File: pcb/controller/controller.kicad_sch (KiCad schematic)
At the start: 16 parts, among them J1 Barrel_Jack, J2 AVR-ISP-6, U1 ATmega328P-A, Y1 Crystal_GND24

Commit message: More Controller Updates
Continuing to work on the controller board schematic
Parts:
- added JBUZZ1: Conn_01x02_Male, Connector_JST:JST_PH_B2B-PH-K_1x02_P2.00mm_Vertical, symbol Connector:Conn_01x02_Male
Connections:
- net GND: now also JBUZZ1.1 (Pin_1)
- net at U1.14 (PB2): now also JBUZZ1.2 (Pin_2)
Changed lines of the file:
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@@
+    (stroke (width 0) (type default) (color 0 0 0 0))
+  )
+  (wire (pts (xy 168.91 43.18) (xy 168.91 63.5))
     (stroke (width 0) (type default) (color 0 0 0 0))
   )
@@
     (stroke (width 0) (type default) (color 0 0 0 0))
   )
+  (wire (pts (xy 205.74 34.29) (xy 205.74 36.83))
+    (stroke (width 0) (type default) (color 0 0 0 0))
+  )
   (wire (pts (xy 180.34 71.12) (xy 180.34 99.06))
     (stroke (width 0) (type default) (color 0 0 0 0))
   )
+  (wire (pts (xy 168.91 63.5) (xy 154.94 63.5))
+    (stroke (width 0) (type default) (color 0 0 0 0))
+  )
   (wire (pts (xy 166.37 31.75) (xy 166.37 60.96))
     (stroke (width 0) (type default) (color 0 0 0 0))
@@
     (stroke (width 0) (type default) (color 0 0 0 0))
   )
+  (wire (pts (xy 168.91 43.18) (xy 203.2 43.18))
+    (stroke (width 0) (type default) (color 0 0 0 0))
+  )
   (wire (pts (xy 154.94 71.12) (xy 180.34 71.12))
     (stroke (width 0) (type default) (color 0 0 0 0))
@@
   )
   (wire (pts (xy 180.34 99.06) (xy 182.88 99.06))
+    (stroke (width 0) (type default) (color 0 0 0 0))
+  )
+  (wire (pts (xy 203.2 34.29) (xy 203.2 43.18))
     (stroke (width 0) (type default) (color 0 0 0 0))
   )
@@
     (pin "1")
   )
+  (symbol (lib_id "Connector:Conn_01x02_Male") (at 205.74 29.21 270) (unit 1)
+    (in_bom yes) (on_board yes) (fields_autoplaced)
+    (property "Reference" "JBUZZ1" (id 0) (at 207.01 28.5749 90)
+      (effects (font (size 1.27 1.27)) (justify left))
+    )
+    (property "Value" "Conn_01x02_Male" (id 1) (at 207.01 31.1149 90)
+      (effects (font (size 1.27 1.27)) (justify left))
+    )
+    (property "Footprint" "Connector_JST:JST_PH_B2B-PH-K_1x02_P2.00mm_Vertical" (id 2) (at 205.74 29.21 0)
+      (effects (font (size 1.27 1.27)) hide)
+    )
+    (property "Datasheet" "~" (id 3) (at 205.74 29.21 0)
+      (effects (font (size 1.27 1.27)) hide)
+    )
+    (pin "1")
+    (pin "2")
+  )
   (symbol (lib_id "power:GND") (at 172.72 34.29 0) (unit 1)
     (in_bom yes) (on_board yes) (fields_autoplaced)
@@
     (pin "3")
   )
+  (symbol (lib_id "power:GND") (at 205.74 36.83 0) (unit 1)
+    (in_bom yes) (on_board yes) (fields_autoplaced)
+    (property "Reference" "#PWR0118" (id 0) (at 205.74 43.18 0)
+      (effects (font (size 1.27 1.27)) hide)
+    )
+    (property "Value" "GND" (id 1) (at 205.74 41.91 0))
+    (property "Footprint" "" (id 2) (at 205.74 36.83 0)
+      (effects (font (size 1.27 1.27)) hide)
+    )
+    (property "Datasheet" "" (id 3) (at 205.74 36.83 0)
+      (effects (font (size 1.27 1.27)) hide)
+    )
+    (pin "1")
+  )
   (symbol (lib_id "Connector:Conn_01x03_Male") (at 234.95 58.42 180) (unit 1)
     (in_bom yes) (on_board yes)
@@
       (reference "#PWR0117") (unit 1) (value "GND") (footprint "")
     )
+    (path "/b5b62e28-9fc8-463e-a7f1-aa7597965c9b"
+      (reference "#PWR0118") (unit 1) (value "GND") (footprint "")
+    )
     (path "/7f74c263-cca2-4e4e-8840-c701f7c98d5f"
       (reference "#PWR0119") (unit 1) (value "+5V") (footprint "")
@@
       (reference "J2") (unit 1) (value "AVR-ISP-6") (footprint "Connector_IDC:IDC-Header_2x03_P2.54mm_Vertical")
     )
+    (path "/6588fbb0-09c1-440c-88e5-9c03bc8e1ab7"
+      (reference "JBUZZ1") (unit 1) (value "Conn_01x02_Male") (footprint "Connector_JST:JST_PH_B2B-PH-K_1x02_P2.00mm_Vertical")
+    )
     (path "/8f4ef035-8269-4652-85c4-8eb26bfa3f71"

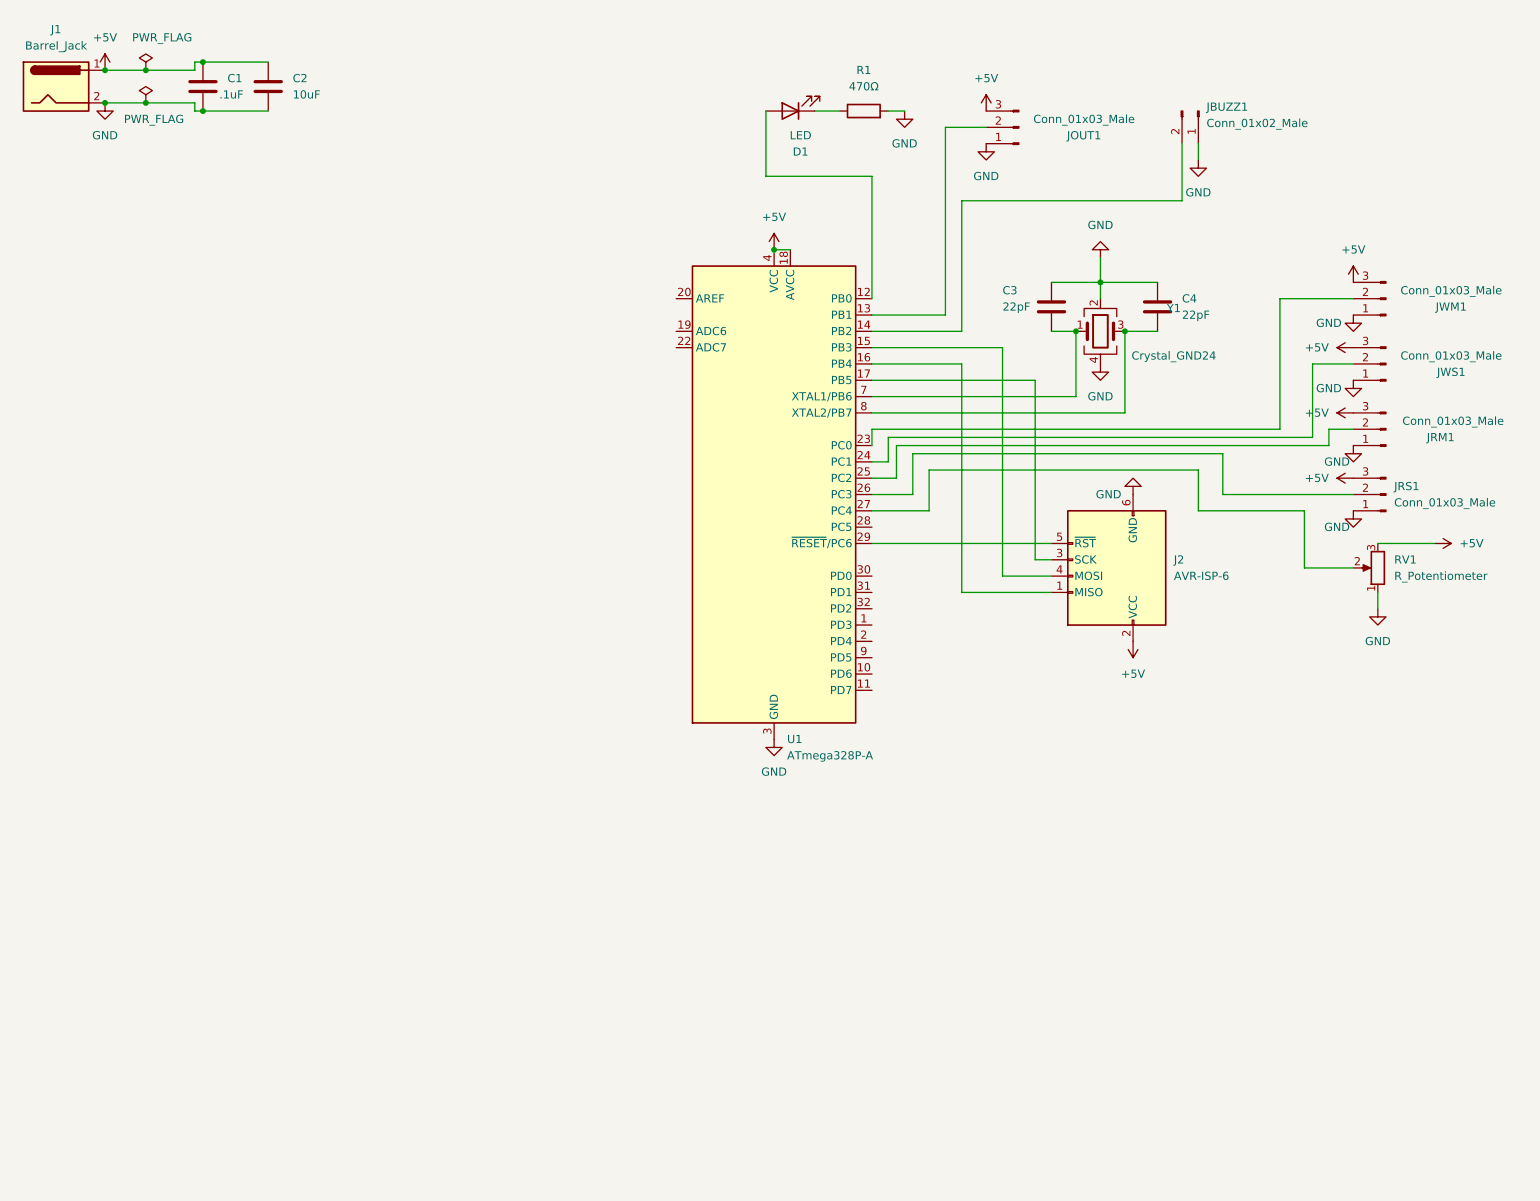
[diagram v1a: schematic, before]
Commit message: First Draft of Control Board
This completes the first draft of the control board schematic, adding
the RF module inputs and the connectors for the start/stop/reset
buttons.
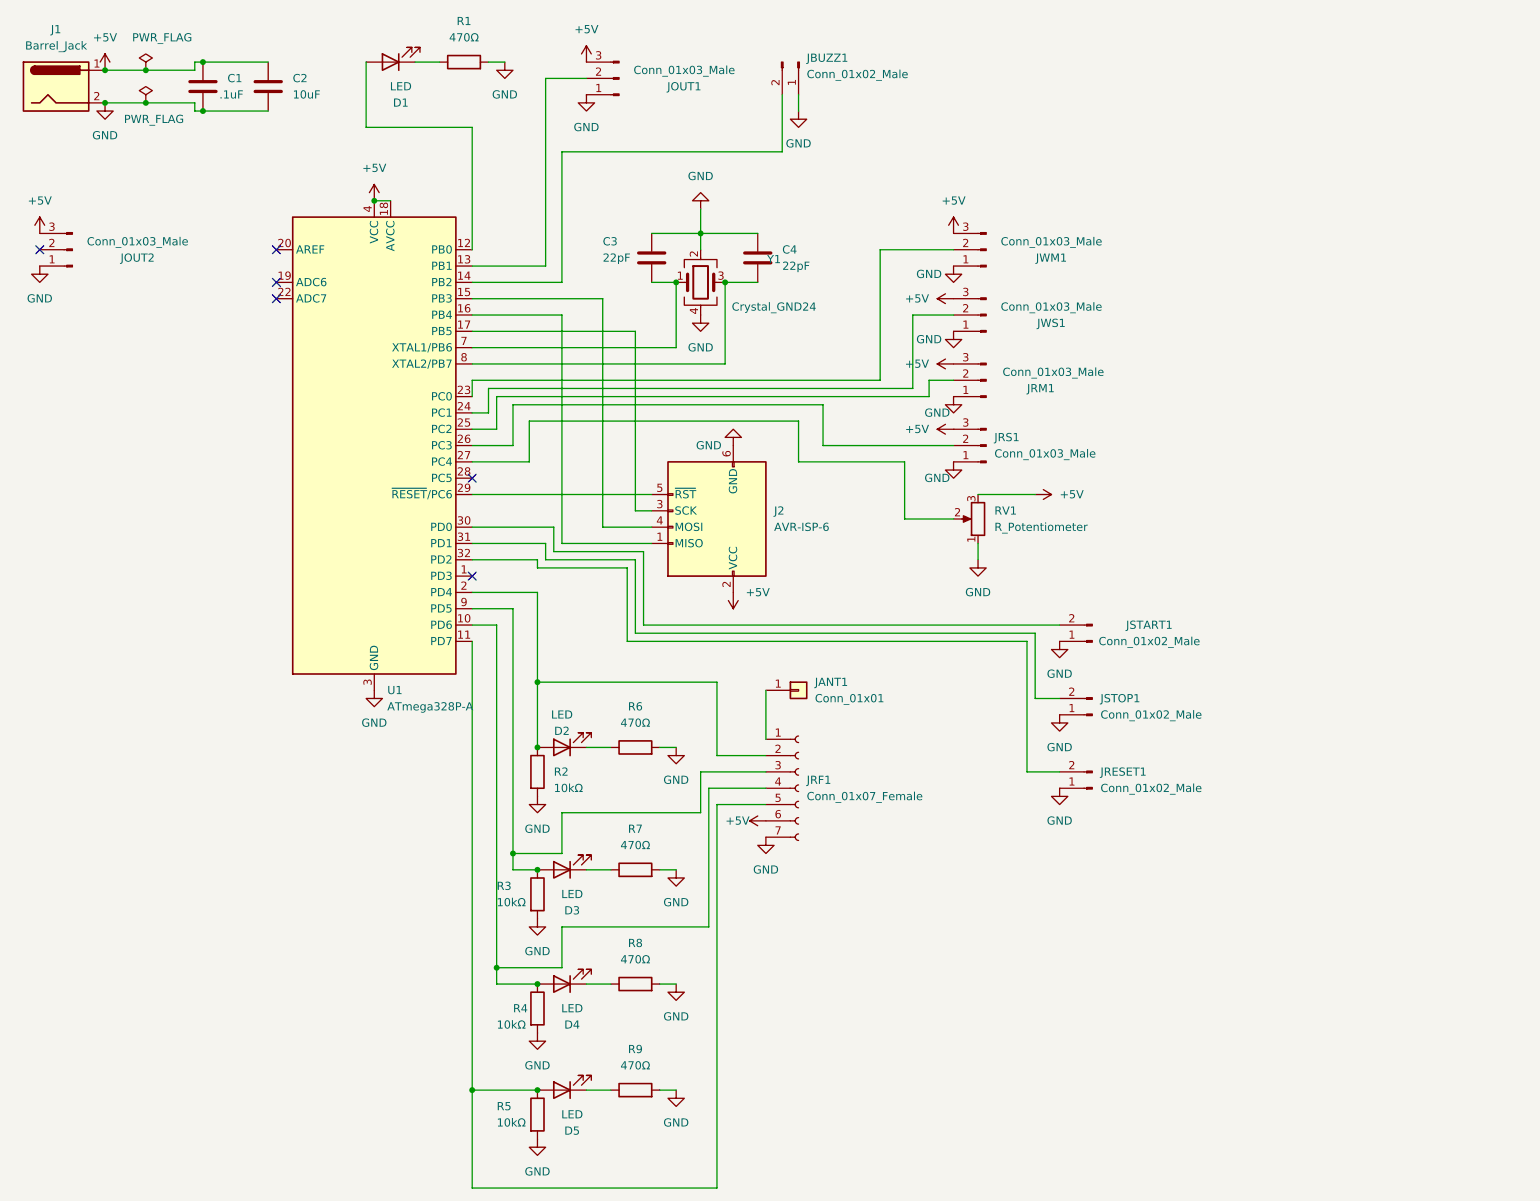
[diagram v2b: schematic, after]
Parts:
- added D2, D3, D4, D5: LED, LED_SMD:LED_0805_2012Metric, symbol Device:LED
- added JANT1: Conn_01x01, Connector_PinHeader_2.54mm:PinHeader_1x01_P2.54mm_Vertical, symbol Connector_Generic:Conn_01x01
- added JOUT2: Conn_01x03_Male, Connector_JST:JST_PH_B3B-PH-K_1x03_P2.00mm_Vertical, symbol Connector:Conn_01x03_Male
- added JRESET1, JSTART1, JSTOP1: Conn_01x02_Male, Connector_JST:JST_PH_B2B-PH-K_1x02_P2.00mm_Vertical, symbol Connector:Conn_01x02_Male
- added JRF1: Conn_01x07_Female, Connector_PinHeader_2.54mm:PinHeader_1x07_P2.54mm_Vertical, symbol Connector:Conn_01x07_Female
- added R2, R3, R4, R5: 10kΩ, Resistor_SMD:R_0603_1608Metric, symbol Device:R
- added R6, R7, R8, R9: 470Ω, Resistor_SMD:R_0805_2012Metric, symbol Device:R
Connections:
- net +5V: now also JOUT2.3 (Pin_3), JRF1.6 (Pin_6)
- net GND: now also JOUT2.1 (Pin_1), JRESET1.1 (Pin_1), JRF1.7 (Pin_7), JSTART1.1 (Pin_1), JSTOP1.1 (Pin_1), R2.2, R3.2, R4.2, R5.2, R6.2, R7.2, R8.2, R9.2
- net at U1.10 (PD6): now also D4.2 (A), JRF1.4 (Pin_4), R4.1
- net at U1.11 (PD7): now also D5.2 (A), JRF1.5 (Pin_5), R5.1
- net at U1.2 (PD4): now also D2.2 (A), JRF1.2 (Pin_2), R2.1
- net at U1.30 (PD0): now also JSTART1.2 (Pin_2)
- net at U1.31 (PD1): now also JSTOP1.2 (Pin_2)
- net at U1.32 (PD2): now also JRESET1.2 (Pin_2)
- net at U1.9 (PD5): now also D3.2 (A), JRF1.3 (Pin_3), R3.1
- new net: D4.1 (K), R8.1
- new net: D3.1 (K), R7.1
- new net: D5.1 (K), R9.1
- new net: JANT1.1 (Pin_1), JRF1.1 (Pin_1)
- new net: D2.1 (K), R6.1
- no-connect marks 0 -> 6
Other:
- moved on the sheet: C3, C4, D1, J2, JBUZZ1, JOUT1, JRM1, JRS1, JWM1, JWS1, R1, RV1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

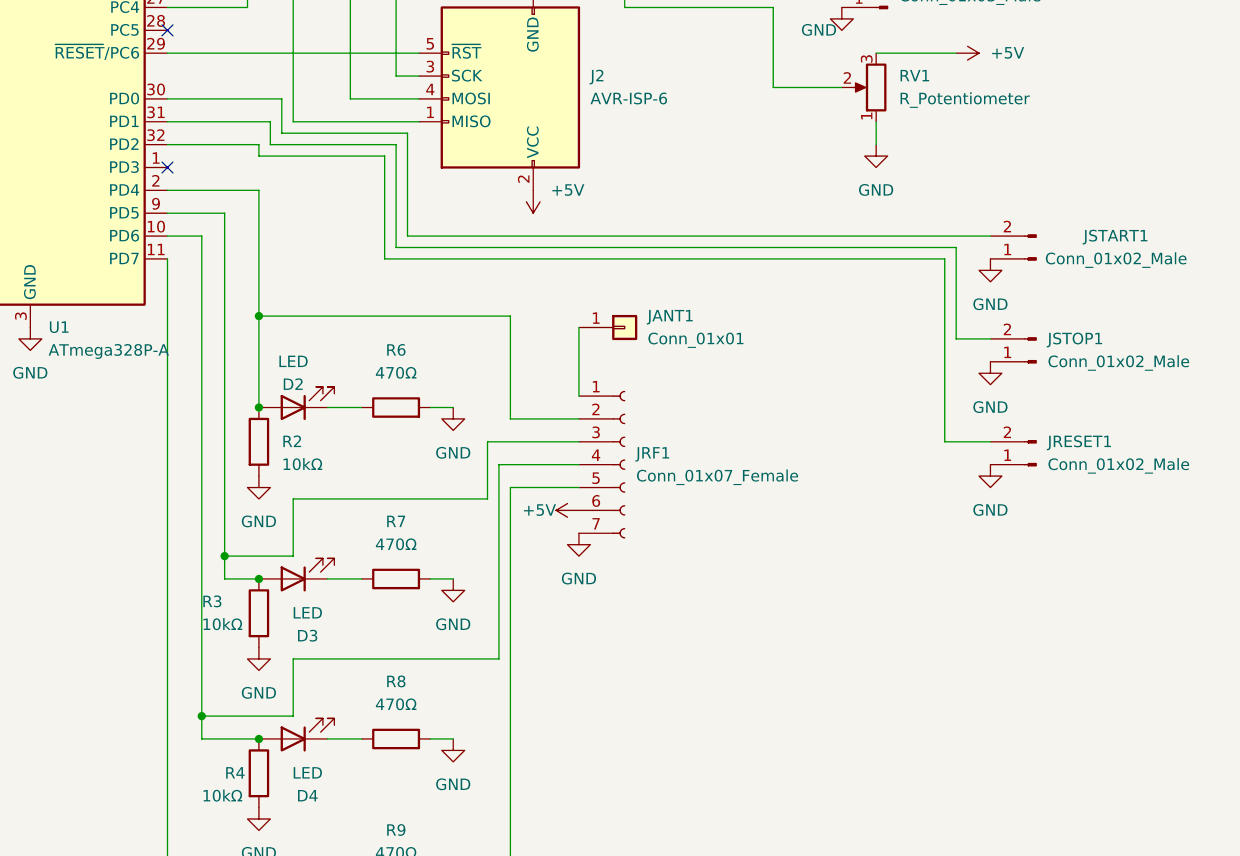
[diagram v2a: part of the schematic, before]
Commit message: Controller PCB Diagnostic Header
This adds a diagnostic header that I'll be able to put a jumper on to
turn on diagnostic mode--which will be used to calibrate the
potentiometer inputs.  In addition to adding this to the PCB layout, I
rearranged a few components and cleaned up some traces.
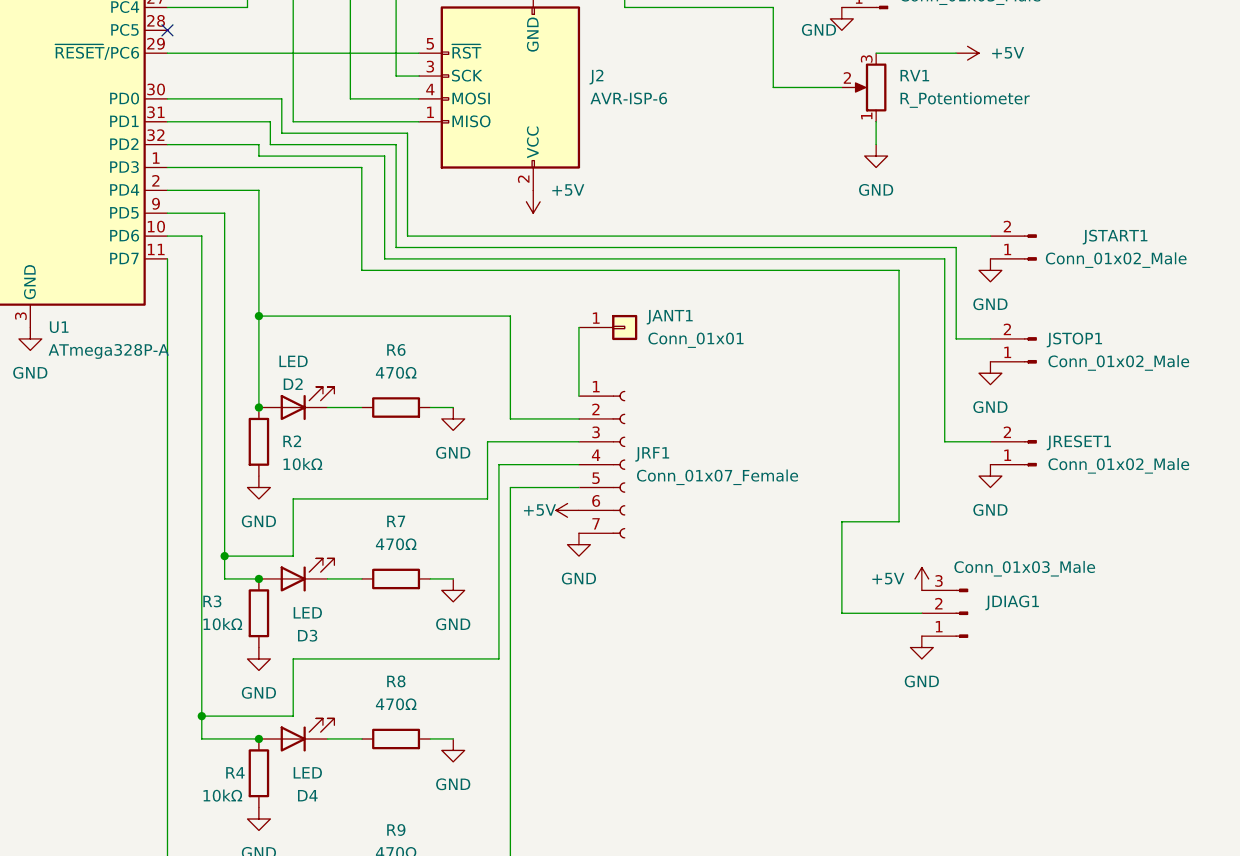
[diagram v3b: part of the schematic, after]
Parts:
- added JDIAG1: Conn_01x03_Male, Connector_PinHeader_2.54mm:PinHeader_1x03_P2.54mm_Vertical, symbol Connector:Conn_01x03_Male
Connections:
- net +5V: now also JDIAG1.3 (Pin_3)
- net GND: now also JDIAG1.1 (Pin_1)
- net at U1.1 (PD3): now also JDIAG1.2 (Pin_2)
- no-connect marks 6 -> 5
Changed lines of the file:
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@@
   (no_connect (at 62.23 55.88))
   (no_connect (at 62.23 50.8))
-  (no_connect (at 92.71 101.6))
   (no_connect (at 92.71 86.36))
+  (wire (pts (xy 114.3 101.6) (xy 92.71 101.6))
+    (stroke (width 0) (type default) (color 0 0 0 0))
+  )
   (wire (pts (xy 124.46 66.04) (xy 124.46 55.88))
     (stroke (width 0) (type default) (color 0 0 0 0))
@@
     (stroke (width 0) (type default) (color 0 0 0 0))
   )
+  (wire (pts (xy 114.3 113.03) (xy 114.3 101.6))
+    (stroke (width 0) (type default) (color 0 0 0 0))
+  )
   (wire (pts (xy 129.54 156.21) (xy 106.68 156.21))
     (stroke (width 0) (type default) (color 0 0 0 0))
@@
     (stroke (width 0) (type default) (color 0 0 0 0))
   )
+  (wire (pts (xy 173.99 113.03) (xy 114.3 113.03))
+    (stroke (width 0) (type default) (color 0 0 0 0))
+  )
   (wire (pts (xy 106.68 156.21) (xy 106.68 162.56))
     (stroke (width 0) (type default) (color 0 0 0 0))
   )
+  (wire (pts (xy 173.99 140.97) (xy 173.99 113.03))
+    (stroke (width 0) (type default) (color 0 0 0 0))
+  )
   (wire (pts (xy 161.29 72.39) (xy 95.25 72.39))
     (stroke (width 0) (type default) (color 0 0 0 0))
@@
     (stroke (width 0) (type default) (color 0 0 0 0))
   )
+  (wire (pts (xy 167.64 140.97) (xy 167.64 151.13))
+    (stroke (width 0) (type default) (color 0 0 0 0))
+  )
   (wire (pts (xy 92.71 68.58) (xy 132.08 68.58))
     (stroke (width 0) (type default) (color 0 0 0 0))
@@
     (stroke (width 0) (type default) (color 0 0 0 0))
   )
+  (wire (pts (xy 167.64 151.13) (xy 176.53 151.13))
+    (stroke (width 0) (type default) (color 0 0 0 0))
+  )
   (wire (pts (xy 96.52 165.1) (xy 96.52 162.56))
     (stroke (width 0) (type default) (color 0 0 0 0))
@@
   )
   (wire (pts (xy 138.43 132.08) (xy 128.27 132.08))
+    (stroke (width 0) (type default) (color 0 0 0 0))
+  )
+  (wire (pts (xy 173.99 140.97) (xy 167.64 140.97))
     (stroke (width 0) (type default) (color 0 0 0 0))
   )
@@
     )
     (pin "1")
+  )
+  (symbol (lib_id "Connector:Conn_01x03_Male") (at 181.61 151.13 180) (unit 1)
+    (in_bom yes) (on_board yes)
+    (property "Reference" "JDIAG1" (id 0) (at 186.69 149.86 0))
+    (property "Value" "Conn_01x03_Male" (id 1) (at 187.96 146.05 0))
+    (property "Footprint" "Connector_PinHeader_2.54mm:PinHeader_1x03_P2.54mm_Vertical" (id 2) (at 181.61 151.13 0)
+      (effects (font (size 1.27 1.27)) hide)
+    )
+    (property "Datasheet" "~" (id 3) (at 181.61 151.13 0)
+      (effects (font (size 1.27 1.27)) hide)
+    )
+    (pin "1")
+    (pin "2")
+    (pin "3")
   )
   (symbol (lib_id "power:+5V") (at 77.47 43.18 0) (unit 1)
@@
     (pin "1")
   )
+  (symbol (lib_id "power:+5V") (at 176.53 148.59 0) (unit 1)
+    (in_bom yes) (on_board yes)
+    (property "Reference" "#PWR0138" (id 0) (at 176.53 152.4 0)
+      (effects (font (size 1.27 1.27)) hide)
+    )
+    (property "Value" "+5V" (id 1) (at 172.72 147.32 0))
+    (property "Footprint" "" (id 2) (at 176.53 148.59 0)
+      (effects (font (size 1.27 1.27)) hide)
+    )
+    (property "Datasheet" "" (id 3) (at 176.53 148.59 0)
+      (effects (font (size 1.27 1.27)) hide)
+    )
+    (pin "1")
+  )
   (symbol (lib_id "power:GND") (at 124.46 165.1 0) (unit 1)
     (in_bom yes) (on_board yes) (fields_autoplaced)
@@
     )
     (property "Datasheet" "" (id 3) (at 102.87 189.23 0)
+      (effects (font (size 1.27 1.27)) hide)
+    )
+    (pin "1")
+  )
+  (symbol (lib_id "power:GND") (at 176.53 153.67 0) (unit 1)
+    (in_bom yes) (on_board yes) (fields_autoplaced)
+    (property "Reference" "#PWR0139" (id 0) (at 176.53 160.02 0)
+      (effects (font (size 1.27 1.27)) hide)
+    )
+    (property "Value" "GND" (id 1) (at 176.53 158.75 0))
+    (property "Footprint" "" (id 2) (at 176.53 153.67 0)
+      (effects (font (size 1.27 1.27)) hide)
+    )
+    (property "Datasheet" "" (id 3) (at 176.53 153.67 0)
       (effects (font (size 1.27 1.27)) hide)
     )
@@
       (reference "#PWR0137") (unit 1) (value "GND") (footprint "")
     )
+    (path "/5ed5e4da-67fd-409c-ada6-63484510164c"
+      (reference "#PWR0138") (unit 1) (value "+5V") (footprint "")
+    )
+    (path "/8becf175-9d14-4edb-bd98-0f6b8dfa7f29"
+      (reference "#PWR0139") (unit 1) (value "GND") (footprint "")
+    )
     (path "/1259f7ab-f73e-40da-888d-1b2ca8d21b4a"
       (reference "C1") (unit 1) (value ".1uF") (footprint "Capacitor_SMD:C_0603_1608Metric")
@@
       (reference "JBUZZ1") (unit 1) (value "Conn_01x02_Male") (footprint "Connector_JST:JST_PH_B2B-PH-K_1x02_P2.00mm_Vertical")
     )
+    (path "/234a19cc-c22a-4567-84d7-c9068458a261"
+      (reference "JDIAG1") (unit 1) (value "Conn_01x03_Male") (footprint "Connector_PinHeader_2.54mm:PinHeader_1x03_P2.54mm_Vertical")
+    )
     (path "/8f4ef035-8269-4652-85c4-8eb26bfa3f71"
